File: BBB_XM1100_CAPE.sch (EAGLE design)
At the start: 24 parts, among them U2 MIC5225-3.3

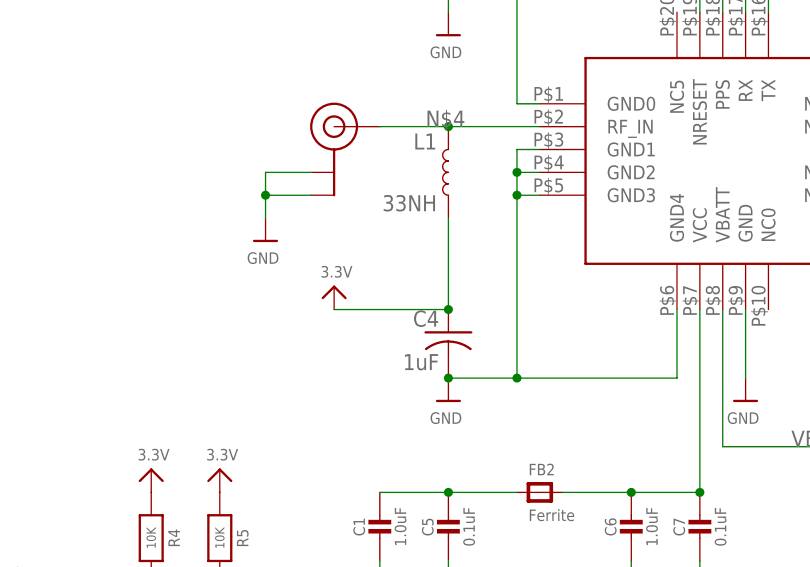
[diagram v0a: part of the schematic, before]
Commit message: BOM updates associated with populating first test boards
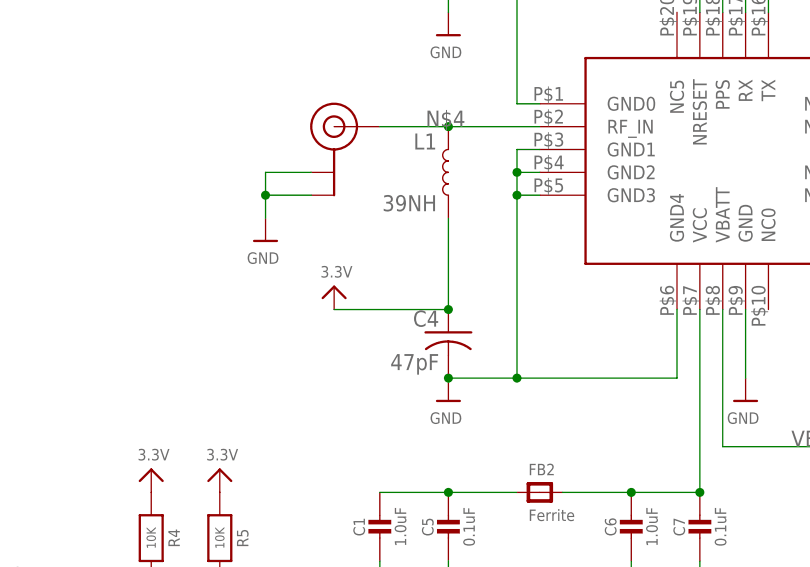
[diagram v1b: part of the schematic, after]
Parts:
- C4: value 1uF -> 47pF
- L1: value 33NH -> 39NH
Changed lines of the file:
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@@
 <part name="U$10" library="microbuilder" deviceset="3.3V" device=""/>
 <part name="GND1" library="supply1" deviceset="GND" device=""/>
-<part name="C4" library="rcl" deviceset="C-US" device="C0805" value="1uF"/>
-<part name="L1" library="SparkFun-Coils" deviceset="INDUCTOR" device="-0402-3.9NH" value="33NH"/>
+<part name="C4" library="rcl" deviceset="C-US" device="C0805" value="47pF"/>
+<part name="L1" library="SparkFun-Coils" deviceset="INDUCTOR" device="-0402-3.9NH" value="39NH"/>
 <part name="U$12" library="microbuilder" deviceset="GND" device=""/>
 <part name="U$17" library="microbuilder" deviceset="3.3V" device=""/>

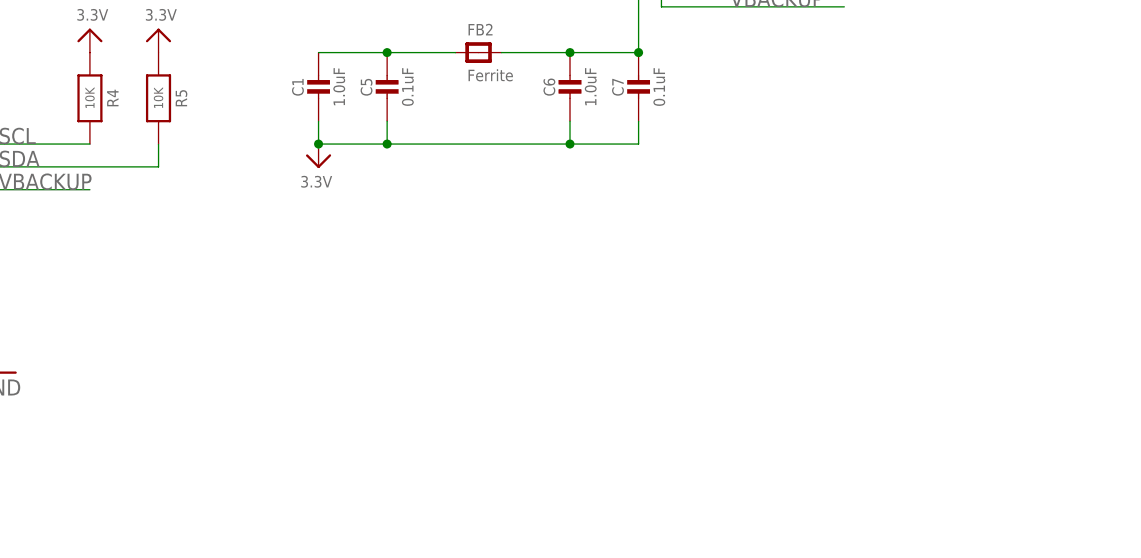
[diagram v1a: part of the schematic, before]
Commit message: added eeprom to XM1100 cape
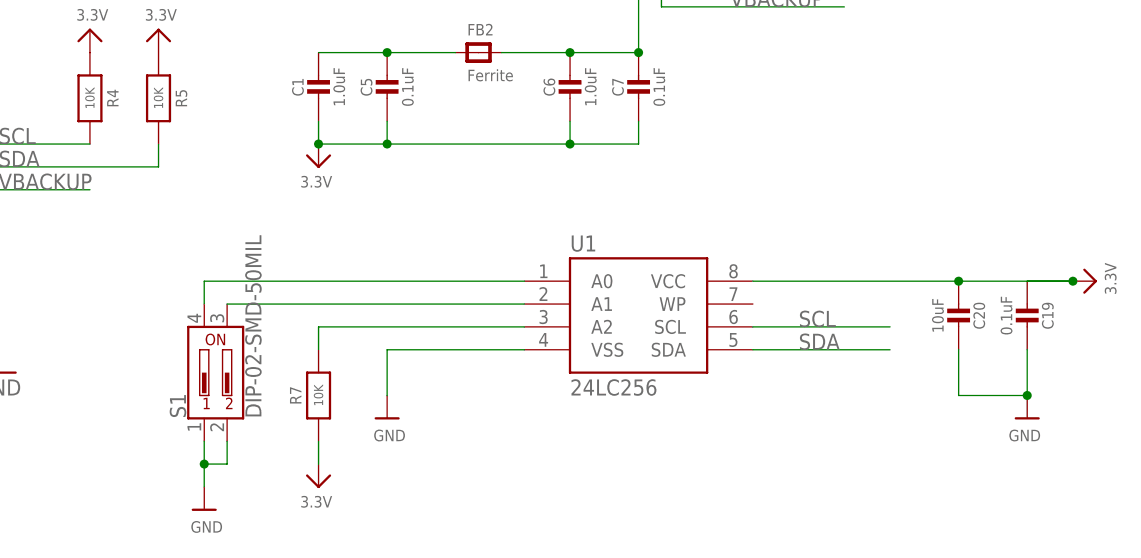
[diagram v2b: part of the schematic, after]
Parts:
- added C19: 0.1uF, microbuilder:CAP_CERAMIC0805-NOOUTLINE
- added C20: 10uF, microbuilder:CAP_CERAMIC0805-NOOUTLINE
- added R7: 10K, microbuilder:RESISTOR0805_NOOUTLINE
- added S1: DIP-02-SMD-50MIL, SparkFun-Switches:DIP-02-SMD-50MIL
- added U1: 24LC256, SparkFun-IC-Memory:EEPROM-I2CSMD
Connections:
- new net N$13: R7.2, U1.A2
- new net N$15: S1.P$11, U1.A1
- new net N$16: S1.P$12, U1.A0
- net 3.3V: now also C19.1, C20.1, R7.1, U1.VCC
- net GND: now also C19.2, C20.2, S1.P$1, S1.P$2, U1.VSS
- net SCL: now also U1.SCL
- net SDA: now also U1.SDA
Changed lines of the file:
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@@
 <part name="R6" library="microbuilder" deviceset="RESISTOR" device="0805_NOOUTLINE" value="10K"/>
 <part name="U$2" library="microbuilder" deviceset="3.3V" device=""/>
+<part name="U1" library="SparkFun-IC-Memory" deviceset="EEPROM-I2C" device="SMD" value="24LC256"/>
+<part name="S1" library="SparkFun-Switches" deviceset="DIP-02" device="-SMD-50MIL"/>
+<part name="U$7" library="microbuilder" deviceset="GND" device=""/>
+<part name="R7" library="microbuilder" deviceset="RESISTOR" device="0805_NOOUTLINE" value="10K"/>
+<part name="U$18" library="microbuilder" deviceset="3.3V" device=""/>
+<part name="U$23" library="microbuilder" deviceset="GND" device=""/>
+<part name="U$25" library="microbuilder" deviceset="GND" device=""/>
+<part name="U$26" library="microbuilder" deviceset="3.3V" device=""/>
+<part name="C19" library="microbuilder" deviceset="CAP_CERAMIC" device="0805-NOOUTLINE" value="0.1uF"/>
+<part name="C20" library="microbuilder" deviceset="CAP_CERAMIC" device="0805-NOOUTLINE" value="10uF"/>
 </parts>
 <sheets>
@@
 <instance part="R6" gate="G$1" x="231.14" y="111.76" rot="MR270"/>
 <instance part="U$2" gate="G$1" x="231.14" y="119.38" rot="MR0"/>
+<instance part="U1" gate="G$1" x="210.82" y="12.7"/>
+<instance part="S1" gate="G$1" x="162.56" y="7.62"/>
+<instance part="U$7" gate="G$1" x="162.56" y="-7.62"/>
+<instance part="R7" gate="G$1" x="175.26" y="5.08" rot="R90"/>
+<instance part="U$18" gate="G$1" x="175.26" y="-5.08" rot="R180"/>
+<instance part="U$23" gate="G$1" x="182.88" y="2.54"/>
+<instance part="U$25" gate="G$1" x="254" y="2.54" rot="MR0"/>
+<instance part="U$26" gate="G$1" x="261.62" y="17.78" rot="MR90"/>
+<instance part="C19" gate="G$1" x="254" y="12.7" rot="MR0"/>
+<instance part="C20" gate="G$1" x="246.38" y="12.7" rot="MR0"/>
 </instances>
 <busses>
@@
 <pinref part="U$4" gate="G$1" pin="GND"/>
 </segment>
+<segment>
+<pinref part="U$7" gate="G$1" pin="GND"/>
+<pinref part="S1" gate="G$1" pin="P$1"/>
+<wire x1="162.56" y1="-5.08" x2="162.56" y2="-2.54" width="0.1524" layer="91"/>
+<pinref part="S1" gate="G$1" pin="P$2"/>
+<wire x1="162.56" y1="-2.54" x2="162.56" y2="0" width="0.1524" layer="91"/>
+<wire x1="165.1" y1="0" x2="165.1" y2="-2.54" width="0.1524" layer="91"/>
+<wire x1="165.1" y1="-2.54" x2="162.56" y2="-2.54" width="0.1524" layer="91"/>
+<junction x="162.56" y="-2.54"/>
+</segment>
+<segment>
+<pinref part="U1" gate="G$1" pin="VSS"/>
+<wire x1="198.12" y1="10.16" x2="182.88" y2="10.16" width="0.1524" layer="91"/>
+<wire x1="182.88" y1="10.16" x2="182.88" y2="5.08" width="0.1524" layer="91"/>
+<pinref part="U$23" gate="G$1" pin="GND"/>
+</segment>
+<segment>
+<pinref part="U$25" gate="G$1" pin="GND"/>
+<pinref part="C19" gate="G$1" pin="2"/>
+<wire x1="254" y1="10.16" x2="254" y2="5.08" width="0.1524" layer="91"/>
+<junction x="254" y="5.08"/>
+<pinref part="C20" gate="G$1" pin="2"/>
+<wire x1="246.38" y1="5.08" x2="254" y2="5.08" width="0.1524" layer="91"/>
+<wire x1="246.38" y1="10.16" x2="246.38" y2="5.08" width="0.1524" layer="91"/>
+</segment>
 </net>
 <net name="3.3V" class="0">
@@
 <pinref part="U$2" gate="G$1" pin="3.3V"/>
 </segment>
+<segment>
+<pinref part="R7" gate="G$1" pin="1"/>
+<pinref part="U$18" gate="G$1" pin="3.3V"/>
+<wire x1="175.26" y1="0" x2="175.26" y2="-2.54" width="0.1524" layer="91"/>
+</segment>
+<segment>
+<pinref part="U$26" gate="G$1" pin="3.3V"/>
+<pinref part="C19" gate="G$1" pin="1"/>
+<junction x="259.08" y="17.78"/>
+<wire x1="246.38" y1="17.78" x2="259.08" y2="17.78" width="0.1524" layer="91"/>
+<wire x1="259.08" y1="17.78" x2="254" y2="17.78" width="0.1524" layer="91"/>
+<pinref part="C20" gate="G$1" pin="1"/>
+<junction x="246.38" y="17.78"/>
+<pinref part="U1" gate="G$1" pin="VCC"/>
+<wire x1="223.52" y1="17.78" x2="246.38" y2="17.78" width="0.1524" layer="91"/>
+</segment>
 </net>
 <net name="ENABLE" class="0">
@@
 <label x="83.82" y="78.74" size="1.778" layer="95"/>
 </segment>
+<segment>
+<pinref part="U1" gate="G$1" pin="SDA"/>
+<wire x1="223.52" y1="10.16" x2="238.76" y2="10.16" width="0.1524" layer="91"/>
+<label x="228.6" y="10.16" size="1.778" layer="95"/>
+</segment>
 </net>
 <net name="SCL" class="0">
@@
 <wire x1="22.86" y1="78.74" x2="7.62" y2="78.74" width="0.1524" layer="91"/>
 <label x="7.62" y="78.74" size="1.778" layer="95"/>
+</segment>
+<segment>
+<pinref part="U1" gate="G$1" pin="SCL"/>
+<wire x1="223.52" y1="12.7" x2="238.76" y2="12.7" width="0.1524" layer="91"/>
+<label x="228.6" y="12.7" size="1.778" layer="95"/>
 </segment>
 </net>
@@
 </segment>
 </net>
+<net name="N$13" class="0">
+<segment>
+<pinref part="U1" gate="G$1" pin="A2"/>
+<wire x1="198.12" y1="12.7" x2="175.26" y2="12.7" width="0.1524" layer="91"/>
+<wire x1="175.26" y1="12.7" x2="175.26" y2="10.16" width="0.1524" layer="91"/>
+<pinref part="R7" gate="G$1" pin="2"/>
+</segment>
+</net>
+<net name="N$15" class="0">
+<segment>
+<pinref part="S1" gate="G$1" pin="P$11"/>
+<pinref part="U1" gate="G$1" pin="A1"/>
+<wire x1="165.1" y1="15.24" x2="198.12" y2="15.24" width="0.1524" layer="91"/>
+</segment>
+</net>
+<net name="N$16" class="0">
+<segment>
+<pinref part="U1" gate="G$1" pin="A0"/>
+<pinref part="S1" gate="G$1" pin="P$12"/>
+<wire x1="198.12" y1="17.78" x2="162.56" y2="17.78" width="0.1524" layer="91"/>
+<wire x1="162.56" y1="17.78" x2="162.56" y2="15.24" width="0.1524" layer="91"/>
+</segment>
+</net>

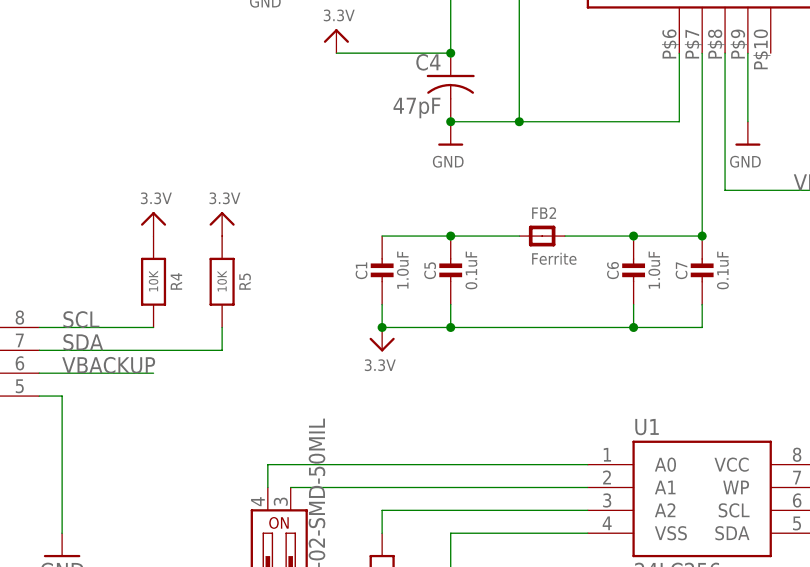
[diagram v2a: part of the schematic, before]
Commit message: corrected error in VCC/GND connections on xm1100 cape
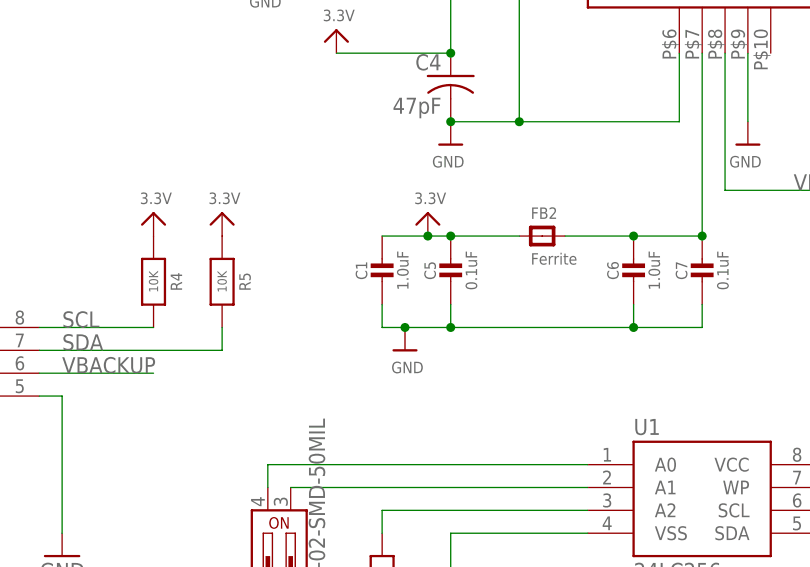
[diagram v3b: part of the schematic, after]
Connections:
- removed net N$2: C1.1, C5.1, FB2.P$1
- net 3.3V: now also C1.1, C5.1, FB2.P$1; no longer C1.2, C5.2, C6.2, C7.2
- net GND: now also C1.2, C5.2, C6.2, C7.2
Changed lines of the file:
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@@
 <part name="U$11" library="microbuilder" deviceset="GND" device=""/>
 <part name="U$4" library="microbuilder" deviceset="GND" device=""/>
-<part name="U$16" library="microbuilder" deviceset="3.3V" device=""/>
 <part name="FB2" library="microbuilder" deviceset="FERRITE" device="-0805NO" value="Ferrite"/>
 <part name="C1" library="microbuilder" deviceset="CAP_CERAMIC" device="0805-NOOUTLINE" value="1.0uF"/>
@@
 <part name="C19" library="microbuilder" deviceset="CAP_CERAMIC" device="0805-NOOUTLINE" value="0.1uF"/>
 <part name="C20" library="microbuilder" deviceset="CAP_CERAMIC" device="0805-NOOUTLINE" value="10uF"/>
+<part name="U$21" library="microbuilder" deviceset="3.3V" device=""/>
+<part name="U$16" library="microbuilder" deviceset="GND" device=""/>
 </parts>
 <sheets>
@@
 <instance part="U$11" gate="G$1" x="182.88" y="93.98" rot="MR0"/>
 <instance part="U$4" gate="G$1" x="215.9" y="53.34" rot="MR0"/>
-<instance part="U$16" gate="G$1" x="175.26" y="30.48" rot="R180"/>
 <instance part="FB2" gate="G$1" x="193.04" y="43.18"/>
 <instance part="C1" gate="G$1" x="175.26" y="38.1"/>
@@
 <instance part="C19" gate="G$1" x="254" y="12.7" rot="MR0"/>
 <instance part="C20" gate="G$1" x="246.38" y="12.7" rot="MR0"/>
+<instance part="U$21" gate="G$1" x="180.34" y="45.72"/>
+<instance part="U$16" gate="G$1" x="177.8" y="30.48"/>
 </instances>
 <busses>
@@
 <wire x1="246.38" y1="10.16" x2="246.38" y2="5.08" width="0.1524" layer="91"/>
 </segment>
-</net>
-<net name="3.3V" class="0">
-<segment>
-<pinref part="R3" gate="G$1" pin="1"/>
-<pinref part="U$13" gate="G$1" pin="3.3V"/>
-<wire x1="213.36" y1="119.38" x2="213.36" y2="124.46" width="0.1524" layer="91"/>
-</segment>
-<segment>
-<pinref part="DS3231" gate="G$1" pin="VCC"/>
-<pinref part="U$8" gate="G$1" pin="3.3V"/>
-</segment>
-<segment>
-<pinref part="R4" gate="G$1" pin="1"/>
-<pinref part="U$9" gate="G$1" pin="3.3V"/>
-</segment>
-<segment>
-<pinref part="R5" gate="G$1" pin="1"/>
-<pinref part="U$10" gate="G$1" pin="3.3V"/>
-</segment>
-<segment>
-<wire x1="228.6" y1="165.1" x2="228.6" y2="162.56" width="0.1524" layer="91"/>
-<wire x1="223.52" y1="165.1" x2="228.6" y2="165.1" width="0.1524" layer="91"/>
-<pinref part="C2" gate="G$1" pin="1"/>
-<pinref part="FB1" gate="G$1" pin="P$2"/>
-<label x="228.6" y="167.64" size="1.778" layer="95"/>
-</segment>
-<segment>
-<pinref part="U$17" gate="G$1" pin="3.3V"/>
-<pinref part="C4" gate="G$1" pin="1"/>
-<wire x1="182.88" y1="63.5" x2="182.88" y2="73.66" width="0.1524" layer="91"/>
-<pinref part="L1" gate="G$1" pin="2"/>
-<wire x1="170.18" y1="63.5" x2="182.88" y2="63.5" width="0.1524" layer="91"/>
-<junction x="182.88" y="63.5"/>
-</segment>
-<segment>
-<pinref part="U$16" gate="G$1" pin="3.3V"/>
+<segment>
 <pinref part="C7" gate="G$1" pin="2"/>
-<wire x1="175.26" y1="33.02" x2="182.88" y2="33.02" width="0.1524" layer="91"/>
+<wire x1="175.26" y1="33.02" x2="177.8" y2="33.02" width="0.1524" layer="91"/>
+<wire x1="177.8" y1="33.02" x2="182.88" y2="33.02" width="0.1524" layer="91"/>
 <wire x1="182.88" y1="33.02" x2="203.2" y2="33.02" width="0.1524" layer="91"/>
 <wire x1="203.2" y1="33.02" x2="210.82" y2="33.02" width="0.1524" layer="91"/>
@@
 <pinref part="C1" gate="G$1" pin="2"/>
 <wire x1="175.26" y1="35.56" x2="175.26" y2="33.02" width="0.1524" layer="91"/>
-<junction x="175.26" y="33.02"/>
+<pinref part="U$16" gate="G$1" pin="GND"/>
+<junction x="177.8" y="33.02"/>
+</segment>
+</net>
+<net name="3.3V" class="0">
+<segment>
+<pinref part="R3" gate="G$1" pin="1"/>
+<pinref part="U$13" gate="G$1" pin="3.3V"/>
+<wire x1="213.36" y1="119.38" x2="213.36" y2="124.46" width="0.1524" layer="91"/>
+</segment>
+<segment>
+<pinref part="DS3231" gate="G$1" pin="VCC"/>
+<pinref part="U$8" gate="G$1" pin="3.3V"/>
+</segment>
+<segment>
+<pinref part="R4" gate="G$1" pin="1"/>
+<pinref part="U$9" gate="G$1" pin="3.3V"/>
+</segment>
+<segment>
+<pinref part="R5" gate="G$1" pin="1"/>
+<pinref part="U$10" gate="G$1" pin="3.3V"/>
+</segment>
+<segment>
+<wire x1="228.6" y1="165.1" x2="228.6" y2="162.56" width="0.1524" layer="91"/>
+<wire x1="223.52" y1="165.1" x2="228.6" y2="165.1" width="0.1524" layer="91"/>
+<pinref part="C2" gate="G$1" pin="1"/>
+<pinref part="FB1" gate="G$1" pin="P$2"/>
+<label x="228.6" y="167.64" size="1.778" layer="95"/>
+</segment>
+<segment>
+<pinref part="U$17" gate="G$1" pin="3.3V"/>
+<pinref part="C4" gate="G$1" pin="1"/>
+<wire x1="182.88" y1="63.5" x2="182.88" y2="73.66" width="0.1524" layer="91"/>
+<pinref part="L1" gate="G$1" pin="2"/>
+<wire x1="170.18" y1="63.5" x2="182.88" y2="63.5" width="0.1524" layer="91"/>
+<junction x="182.88" y="63.5"/>
 </segment>
 <segment>
@@
 <wire x1="223.52" y1="17.78" x2="246.38" y2="17.78" width="0.1524" layer="91"/>
 </segment>
+<segment>
+<pinref part="C1" gate="G$1" pin="1"/>
+<pinref part="C5" gate="G$1" pin="1"/>
+<wire x1="175.26" y1="43.18" x2="180.34" y2="43.18" width="0.1524" layer="91"/>
+<pinref part="FB2" gate="G$1" pin="P$1"/>
+<wire x1="180.34" y1="43.18" x2="182.88" y2="43.18" width="0.1524" layer="91"/>
+<wire x1="182.88" y1="43.18" x2="190.5" y2="43.18" width="0.1524" layer="91"/>
+<junction x="182.88" y="43.18"/>
+<pinref part="U$21" gate="G$1" pin="3.3V"/>
+<junction x="180.34" y="43.18"/>
+</segment>
 </net>
 <net name="ENABLE" class="0">
@@
 </segment>
 </net>
-<net name="N$2" class="0">
-<segment>
-<pinref part="C1" gate="G$1" pin="1"/>
-<pinref part="C5" gate="G$1" pin="1"/>
-<wire x1="175.26" y1="43.18" x2="182.88" y2="43.18" width="0.1524" layer="91"/>
-<pinref part="FB2" gate="G$1" pin="P$1"/>
-<wire x1="182.88" y1="43.18" x2="190.5" y2="43.18" width="0.1524" layer="91"/>
-<junction x="182.88" y="43.18"/>
-</segment>
-</net>
